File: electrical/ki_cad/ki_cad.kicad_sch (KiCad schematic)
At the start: 14 parts, among them M1 Motor_DC, M2 Motor_Servo_Grapner_JR, U1 SeeeduinoXIAO, U2 DRV8833PWP, U3 RFM95W-868S2

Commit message: Suspension Progress
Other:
- note added: "1.3"
- note added: "12 Feb 2024"
- note added: "Hot Wheel Car Circuit"
- moved on the sheet: C1, C2, C3, D3, M1, R2, U2, U3

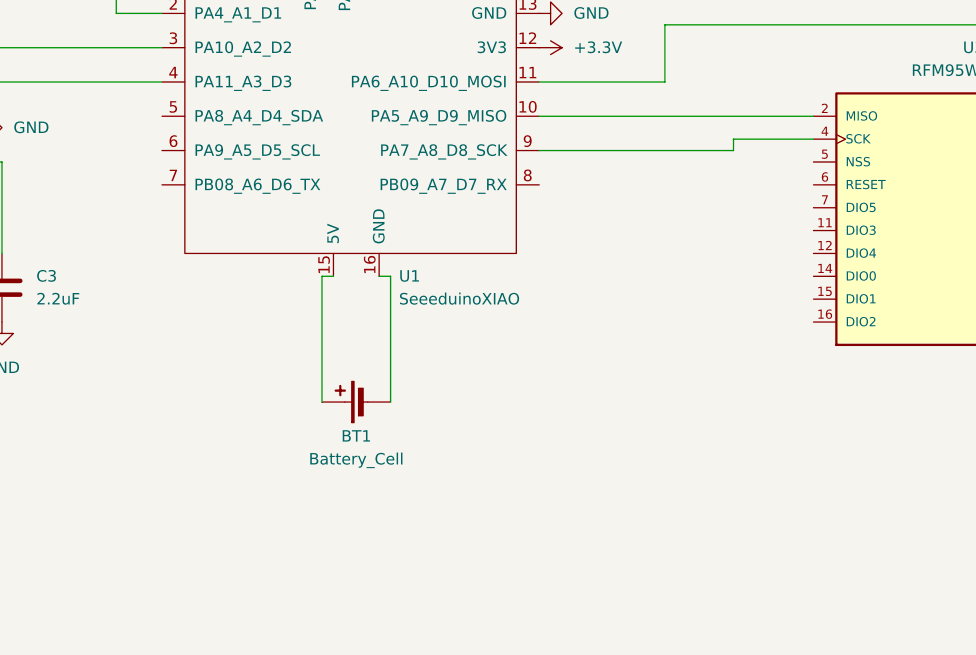
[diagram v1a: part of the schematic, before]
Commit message: added reset and nss pins
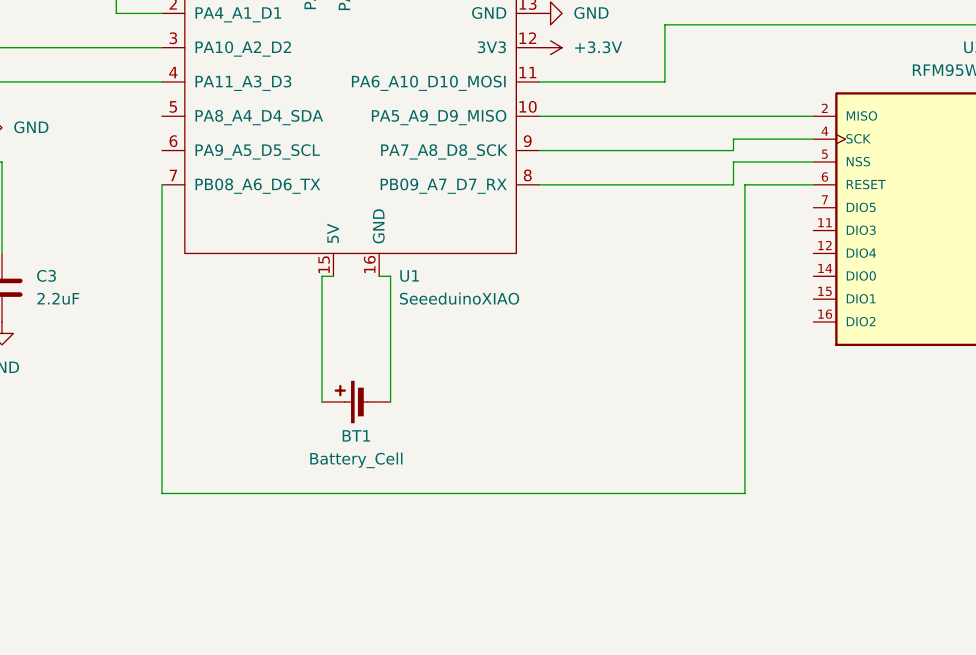
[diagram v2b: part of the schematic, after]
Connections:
- net at U3.5 (NSS): now also U1.8 (PB09_A7_D7_RX)
- net at U3.6 (RESET): now also U1.7 (PB08_A6_D6_TX)
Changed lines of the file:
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@@
+    (stroke (width 0) (type default))
+  )
+  (wire (pts (xy 207.01 139.7) (xy 142.24 139.7))
+    (stroke (width 0) (type default))
+  )
+  (wire (pts (xy 214.63 102.87) (xy 205.74 102.87))
     (stroke (width 0) (type default))
   )
@@
   )
   (wire (pts (xy 198.12 87.63) (xy 265.43 87.63))
+    (stroke (width 0) (type default))
+  )
+  (wire (pts (xy 205.74 105.41) (xy 184.15 105.41))
     (stroke (width 0) (type default))
   )
@@
     (stroke (width 0) (type default))
   )
+  (wire (pts (xy 214.63 105.41) (xy 207.01 105.41))
+    (stroke (width 0) (type default))
+  )
   (wire (pts (xy 96.52 124.46) (xy 102.87 124.46))
+    (stroke (width 0) (type default))
+  )
+  (wire (pts (xy 142.24 139.7) (xy 142.24 105.41))
+    (stroke (width 0) (type default))
+  )
+  (wire (pts (xy 205.74 102.87) (xy 205.74 105.41))
     (stroke (width 0) (type default))
   )
@@
     (stroke (width 0) (type default))
   )
+  (wire (pts (xy 207.01 105.41) (xy 207.01 139.7))
+    (stroke (width 0) (type default))
+  )

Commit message: updated schematic
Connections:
- net at D1.2 (A): now also U1.3 (PA10_A2_D2); no longer U1.2 (PA4_A1_D1)
- net at M2.1 (PWM): now also U1.4 (PA11_A3_D3); no longer U1.1 (PA02_A0_D0)
- net at U2.15 (AIN2): now also U1.1 (PA02_A0_D0); no longer U1.3 (PA10_A2_D2)
- net at U2.16 (AIN1): now also U1.2 (PA4_A1_D1); no longer U1.4 (PA11_A3_D3)
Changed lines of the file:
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@@
   (junction (at 91.44 116.84) (diameter 0) (color 0 0 0 0)
+  )
+  (wire (pts (xy 120.65 92.71) (xy 139.7 92.71))
+    (stroke (width 0) (type default))
   )
   (wire (pts (xy 91.44 116.84) (xy 90.17 116.84))
@@
   )
   (wire (pts (xy 120.65 97.79) (xy 120.65 99.06))
-    (stroke (width 0) (type default))
-  )
-  (wire (pts (xy 120.65 92.71) (xy 121.92 92.71))
     (stroke (width 0) (type default))
   )
@@
     (stroke (width 0) (type default))
   )
+  (wire (pts (xy 137.16 90.17) (xy 142.24 90.17))
+    (stroke (width 0) (type default))
+  )
   (wire (pts (xy 184.15 93.98) (xy 198.12 93.98))
     (stroke (width 0) (type default))
@@
     (stroke (width 0) (type default))
   )
-  (wire (pts (xy 121.92 92.71) (xy 121.92 93.98))
+  (wire (pts (xy 133.35 93.98) (xy 142.24 93.98))
     (stroke (width 0) (type default))
   )
@@
     (stroke (width 0) (type default))
   )
-  (wire (pts (xy 120.65 90.17) (xy 142.24 90.17))
+  (wire (pts (xy 139.7 86.36) (xy 142.24 86.36))
     (stroke (width 0) (type default))
   )
@@
     (stroke (width 0) (type default))
   )
-  (wire (pts (xy 137.16 86.36) (xy 142.24 86.36))
+  (wire (pts (xy 120.65 90.17) (xy 132.08 90.17))
+    (stroke (width 0) (type default))
+  )
+  (wire (pts (xy 132.08 90.17) (xy 132.08 82.55))
     (stroke (width 0) (type default))
   )
@@
     (stroke (width 0) (type default))
   )
-  (wire (pts (xy 142.24 57.15) (xy 142.24 82.55))
-    (stroke (width 0) (type default))
-  )
   (wire (pts (xy 120.65 99.06) (xy 120.65 100.33))
     (stroke (width 0) (type default))
   )
-  (wire (pts (xy 137.16 48.26) (xy 137.16 86.36))
+  (wire (pts (xy 137.16 48.26) (xy 137.16 90.17))
     (stroke (width 0) (type default))
   )
   (wire (pts (xy 214.63 105.41) (xy 207.01 105.41))
+    (stroke (width 0) (type default))
+  )
+  (wire (pts (xy 132.08 82.55) (xy 142.24 82.55))
     (stroke (width 0) (type default))
   )
@@
     (stroke (width 0) (type default))
   )
-  (wire (pts (xy 121.92 93.98) (xy 142.24 93.98))
-    (stroke (width 0) (type default))
-  )
   (wire (pts (xy 205.74 100.33) (xy 214.63 100.33))
     (stroke (width 0) (type default))
@@
     (stroke (width 0) (type default))
   )
-  (wire (pts (xy 156.21 57.15) (xy 142.24 57.15))
+  (wire (pts (xy 133.35 57.15) (xy 156.21 57.15))
     (stroke (width 0) (type default))
   )
@@
     (stroke (width 0) (type default))
   )
+  (wire (pts (xy 133.35 57.15) (xy 133.35 93.98))
+    (stroke (width 0) (type default))
+  )
   (wire (pts (xy 184.15 97.79) (xy 214.63 97.79))
     (stroke (width 0) (type default))
   )
+  (wire (pts (xy 139.7 92.71) (xy 139.7 86.36))
+    (stroke (width 0) (type default))
+  )
